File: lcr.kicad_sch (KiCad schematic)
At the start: 48 parts, among them J1 Conn_01x04_Pin, J6 USB_C_Receptacle_USB2.0_14P, SW1 SW_Push, SW2 SW_Push, U2 UMW HT7836-A, U5 STM32G431CBT6, U8 TLV757P, U9 USBLC6-2SC6, Y2 8 MHz

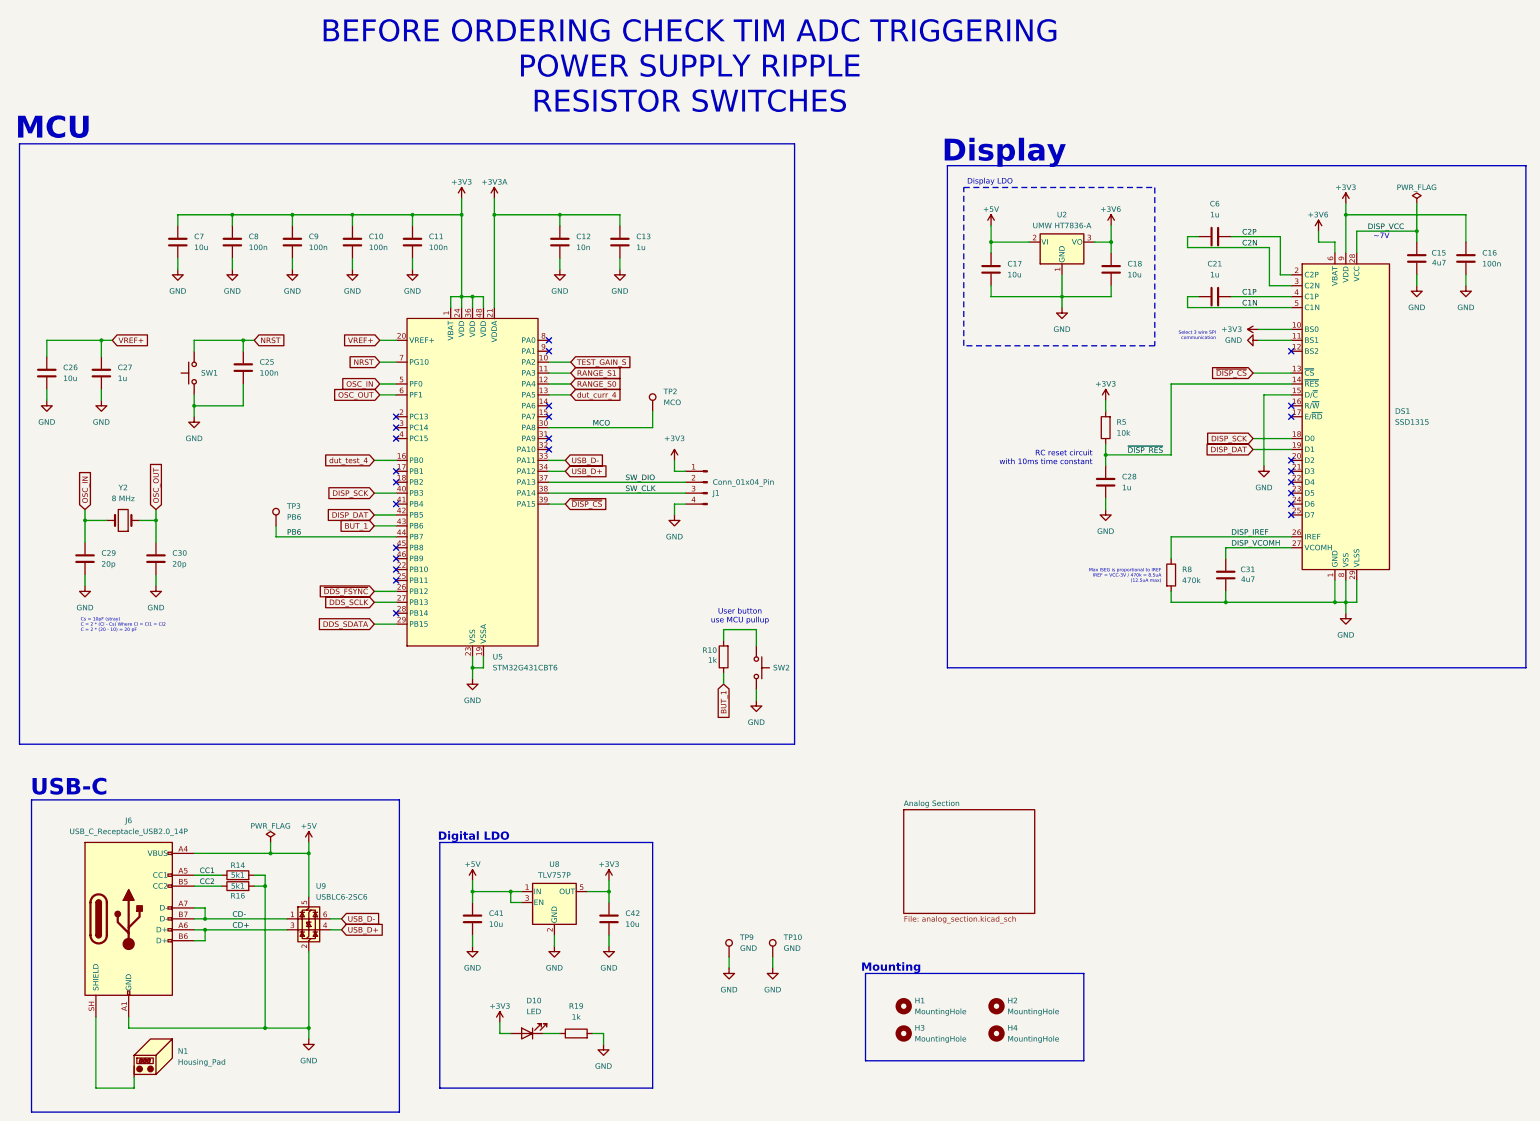
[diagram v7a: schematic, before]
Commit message: Added gate drive current limiting resistors
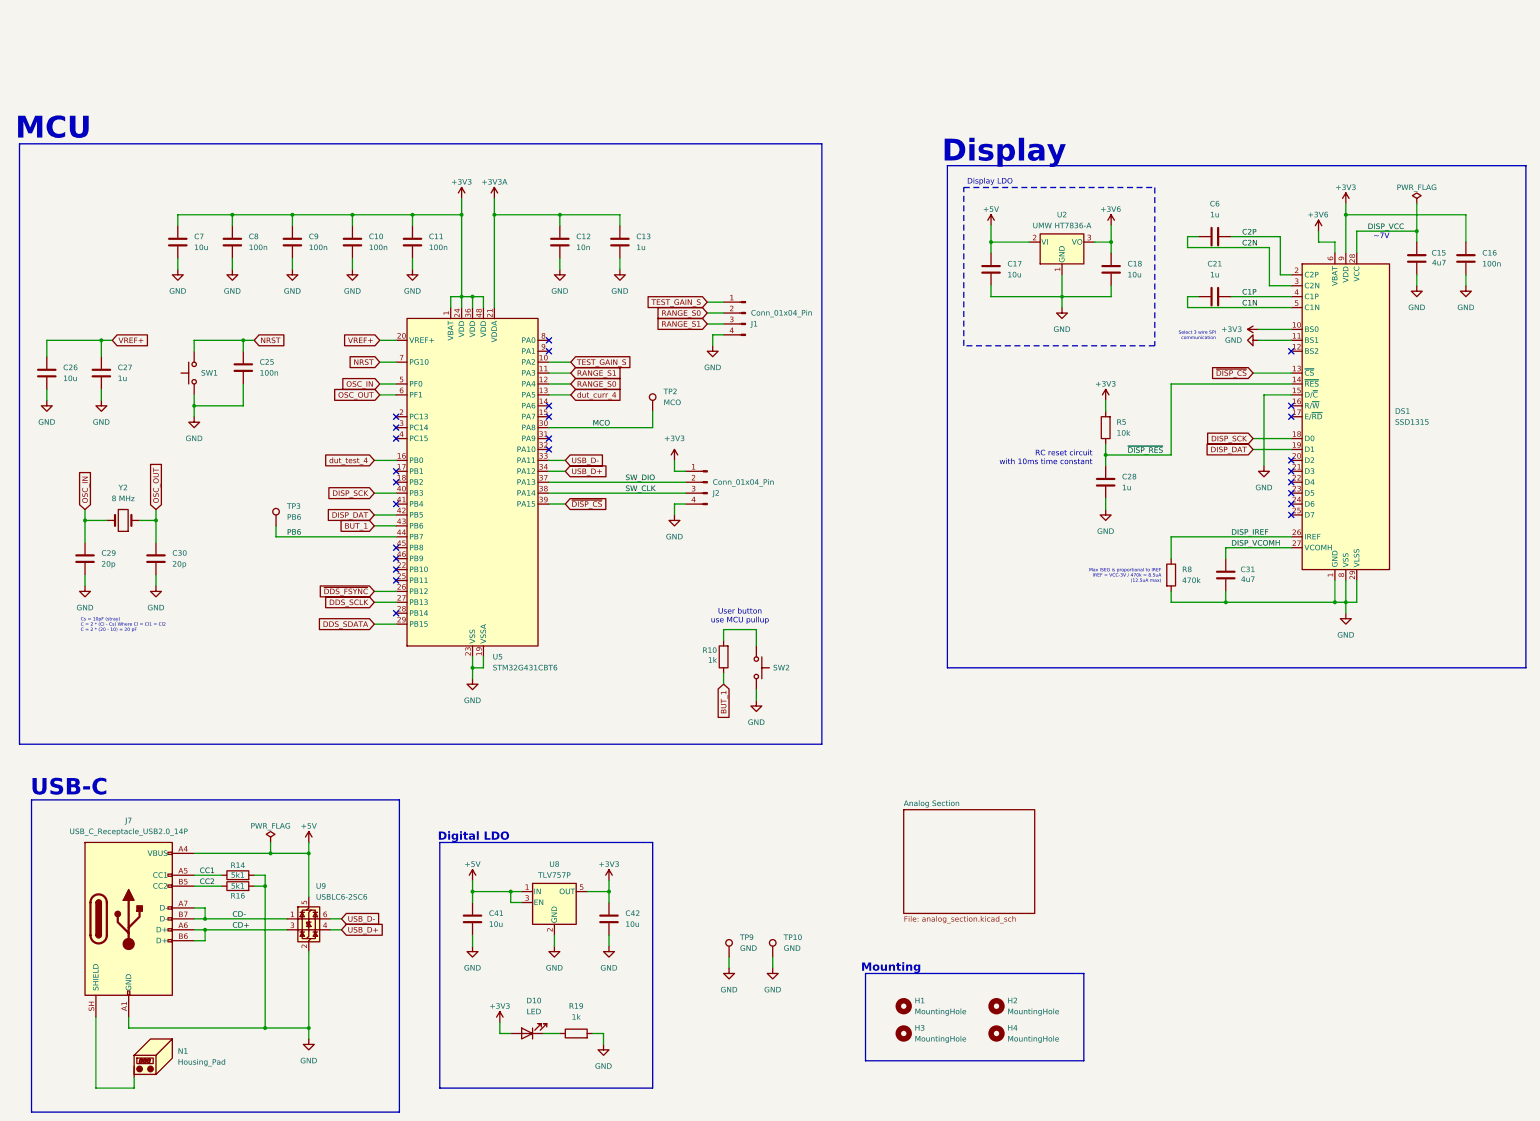
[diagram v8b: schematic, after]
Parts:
- added J1: Conn_01x04_Pin, Connector_PinHeader_2.54mm:PinHeader_1x04_P2.54mm_Vertical, symbol Connector:Conn_01x04_Pin
- C17, C18, C26, C41, C42, C7: Already Have 0 -> 1
- J2: renamed from J1; now left out of the parts list
- renumbered J6 to J7
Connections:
- net GND: now also J1.4 (Pin_4)
- net RANGE_S0: now also J1.2 (Pin_2)
- net RANGE_S1: now also J1.3 (Pin_3)
- net TEST_GAIN_S: now also J1.1 (Pin_1)
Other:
- note removed: "BEFORE ORDERING CHECK TIM ADC TRIGGERING POWER SUPPLY RIPPLE RESISTOR SWITCHES"
